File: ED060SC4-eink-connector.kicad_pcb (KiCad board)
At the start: 2 copper layers, 34.9 x 101.6 mm, 2 parts, among them J1 ED060SC4, J2 Conn_01x39_Pin

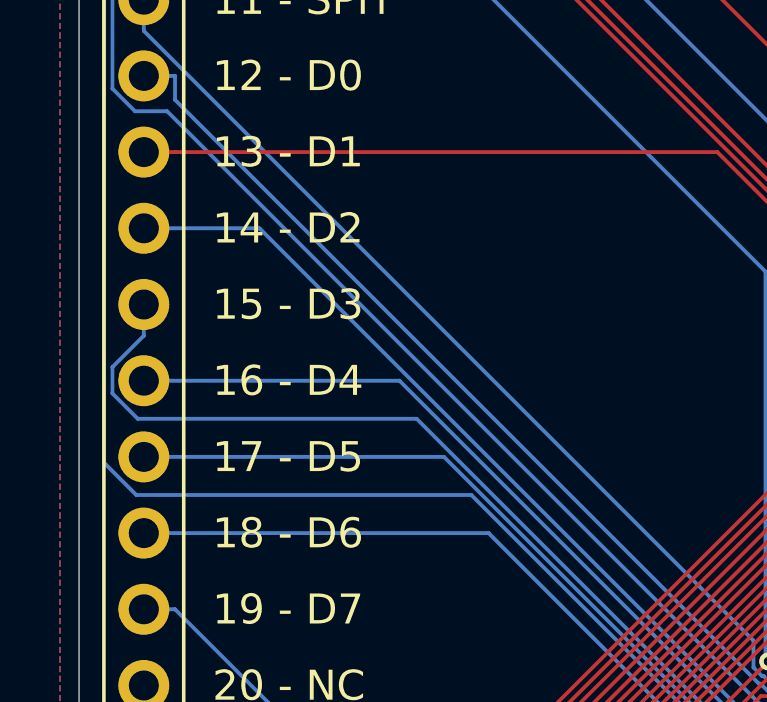
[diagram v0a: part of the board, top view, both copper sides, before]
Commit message: Add a few vias for ground plane
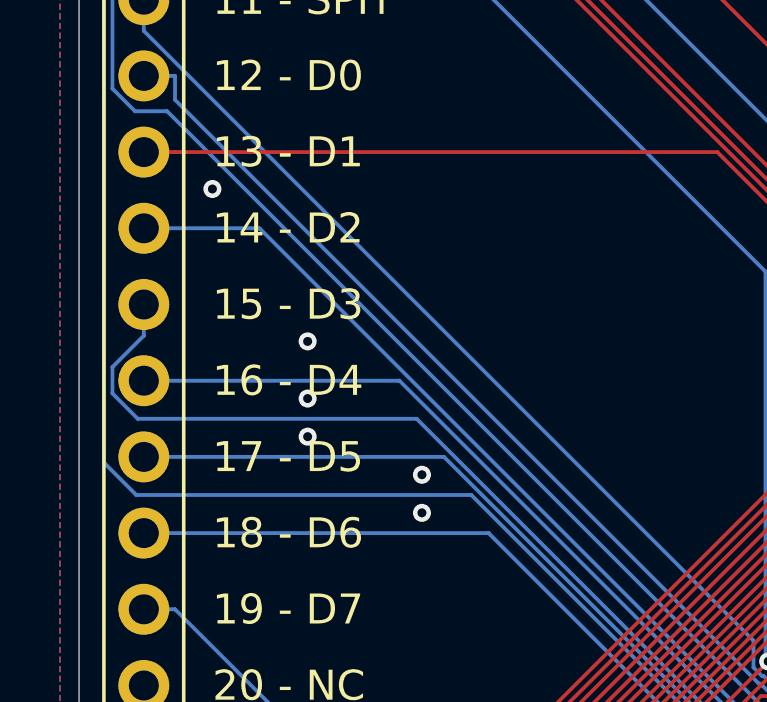
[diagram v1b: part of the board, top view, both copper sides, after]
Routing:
- net /GND: vias 4 -> 10
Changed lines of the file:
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@@
   (segment (start 137.8341 78.9707) (end 137.8341 93.1065) (width 0.127) (layer "F.Cu") (net 6))
   (segment (start 106.934 47.03) (end 106.934 48.0706) (width 0.127) (layer "F.Cu") (net 6))
+  (via (at 116.205 84.455) (size 0.6) (drill 0.3) (layers "F.Cu" "B.Cu") (free) (net 6))
   (via (at 120.65 114.935) (size 0.6) (drill 0.3) (layers "F.Cu" "B.Cu") (free) (net 6))
   (via (at 132.715 67.31) (size 0.6) (drill 0.3) (layers "F.Cu" "B.Cu") (free) (net 6))
+  (via (at 112.395 80.645) (size 0.6) (drill 0.3) (layers "F.Cu" "B.Cu") (free) (net 6))
   (via (at 120.015 113.03) (size 0.6) (drill 0.3) (layers "F.Cu" "B.Cu") (free) (net 6))
+  (via (at 112.395 78.74) (size 0.6) (drill 0.3) (layers "F.Cu" "B.Cu") (free) (net 6))
+  (via (at 116.205 83.185) (size 0.6) (drill 0.3) (layers "F.Cu" "B.Cu") (free) (net 6))
+  (via (at 109.22 73.66) (size 0.6) (drill 0.3) (layers "F.Cu" "B.Cu") (free) (net 6))
+  (via (at 112.395 81.915) (size 0.6) (drill 0.3) (layers "F.Cu" "B.Cu") (free) (net 6))
   (via (at 118.11 112.395) (size 0.6) (drill 0.3) (layers "F.Cu" "B.Cu") (free) (net 6))
   (segment (start 105.8933 42.929) (end 105.8933 40.9464) (width 0.127) (layer "F.Cu") (net 7))

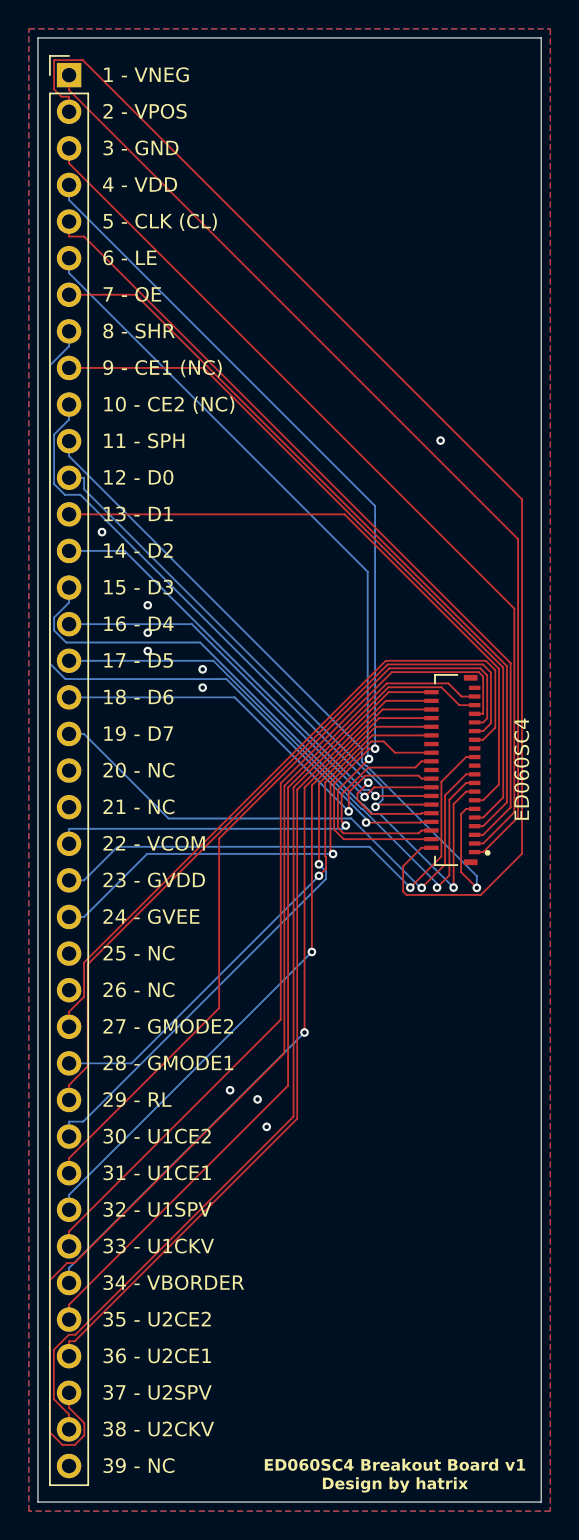
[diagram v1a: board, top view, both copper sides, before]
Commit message: Add mounting holes
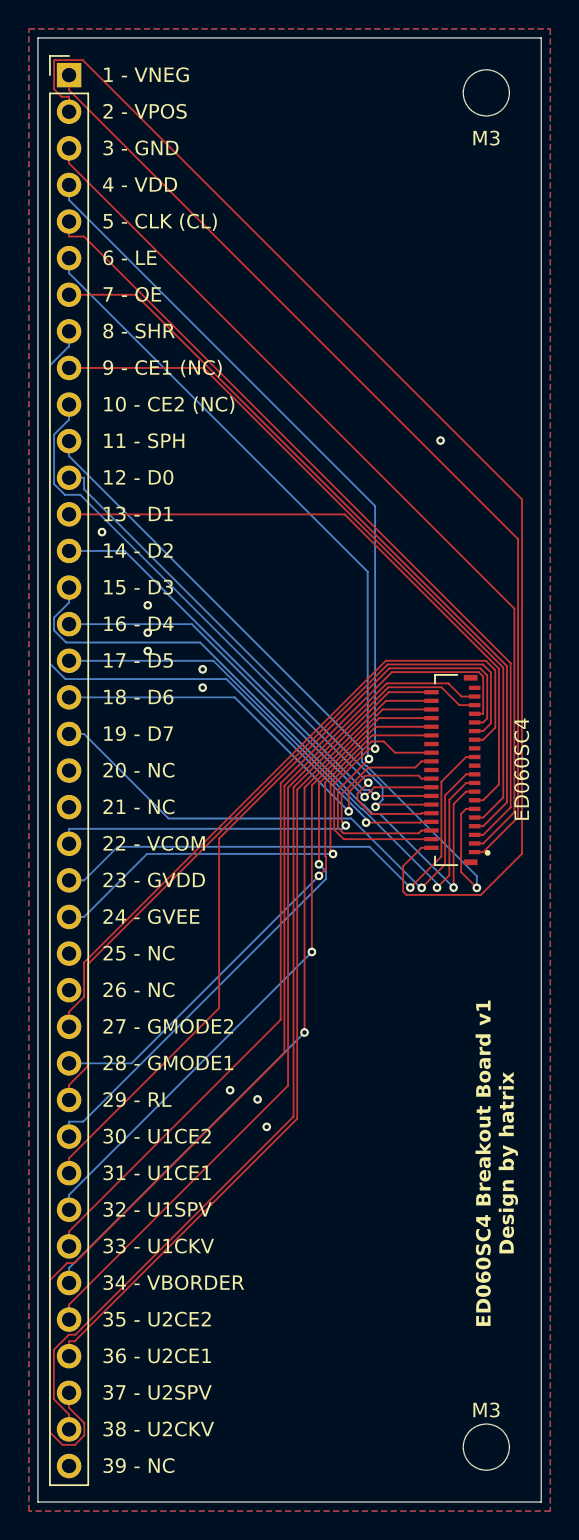
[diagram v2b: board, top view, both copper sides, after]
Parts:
- added M3: MountingHole_3.2mm_M3, MountingHole:MountingHole_3.2mm_M3, F.Cu at (135.9, 137.2)
- added M3: MountingHole_3.2mm_M3, MountingHole:MountingHole_3.2mm_M3, F.Cu at (135.9, 43.2)
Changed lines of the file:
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@@
     )
+  )
+  (footprint "MountingHole:MountingHole_3.2mm_M3" (layer "F.Cu")
+    (at 135.89 137.16)
+    (descr "Mounting Hole 3.2mm, no annular, M3")
+    (tags "mounting hole 3.2mm no annular m3")
+    (attr exclude_from_pos_files exclude_from_bom)
+    (fp_text reference "M3" (at 0 -2.54) (layer "F.SilkS")
+        (effects (font (size 1 1) (thickness 0.15)))
+    )
+    (fp_text value "MountingHole_3.2mm_M3" (at 0 4.2) (layer "F.Fab") hide
+        (effects (font (size 1 1) (thickness 0.15)))
+    )
+    (fp_text user "${REFERENCE}" (at 0 0) (layer "F.Fab")
+        (effects (font (size 1 1) (thickness 0.15)))
+    )
+    (fp_circle (center 0 0) (end 3.2 0)
+      (stroke (width 0.15) (type solid)) (fill none) (layer "Cmts.User"))
+    (fp_circle (center 0 0) (end 3.45 0)
+      (stroke (width 0.05) (type solid)) (fill none) (layer "F.CrtYd"))
+    (pad "" np_thru_hole circle (at 0 0) (size 3.2 3.2) (drill 3.2) (layers "*.Cu" "*.Mask"))
+  )
+  (footprint "MountingHole:MountingHole_3.2mm_M3" (layer "F.Cu")
+    (at 135.89 43.18)
+    (descr "Mounting Hole 3.2mm, no annular, M3")
+    (tags "mounting hole 3.2mm no annular m3")
+    (attr exclude_from_pos_files exclude_from_bom)
+    (fp_text reference "M3" (at 0 3.175) (layer "F.SilkS")
+        (effects (font (size 1 1) (thickness 0.15)))
+    )
+    (fp_text value "MountingHole_3.2mm_M3" (at 0 4.2) (layer "F.Fab") hide
+        (effects (font (size 1 1) (thickness 0.15)))
+    )
+    (fp_text user "${REFERENCE}" (at 0 0) (layer "F.Fab")
+        (effects (font (size 1 1) (thickness 0.15)))
+    )
+    (fp_circle (center 0 0) (end 3.2 0)
+      (stroke (width 0.15) (type solid)) (fill none) (layer "Cmts.User"))
+    (fp_circle (center 0 0) (end 3.45 0)
+      (stroke (width 0.05) (type solid)) (fill none) (layer "F.CrtYd"))
+    (pad "" np_thru_hole circle (at 0 0) (size 3.2 3.2) (drill 3.2) (layers "*.Cu" "*.Mask"))
   )
   (footprint "Connector_PinHeader_2.54mm:PinHeader_1x39_P2.54mm_Vertical" (layer "F.Cu")
@@
     (effects (font (size 1 1) (thickness 0.15)) (justify left bottom))
   )
-  (gr_text "ED060SC4 Breakout Board v1\nDesign by hatrix" (at 129.54 139.065) (layer "F.SilkS")
-    (effects (font (size 0.8 0.8) (thickness 0.2) bold))
+  (gr_text "ED060SC4 Breakout Board v1\nDesign by hatrix" (at 136.525 117.475 90) (layer "F.SilkS")
+    (effects (font (size 1 1) (thickness 0.2) bold))
   )
   (gr_text "13 - D1" (at 109.22 73.025) (layer "F.SilkS")

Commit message: Add original datasheet name for PIN3 (VSS & GND)
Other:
- board text added: "3 - GND (VSS)"
- board text removed: "3 - GND"
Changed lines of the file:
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@@
     (effects (font (size 1 1) (thickness 0.15)) (justify left bottom))
   )
-  (gr_text "3 - GND" (at 109.22 47.625) (layer "F.SilkS")
+  (gr_text "3 - GND (VSS)" (at 109.22 47.625) (layer "F.SilkS")
     (effects (font (size 1 1) (thickness 0.15)) (justify left bottom))
   )

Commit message: Add custom location for JLCPCB's order number
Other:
- board text added: "JLCJLCJLCJLC"
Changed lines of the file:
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@@
       (psa4output false)
       (plotreference true)
-      (plotvalue false)
+      (plotvalue true)
       (plotinvisibletext false)
       (sketchpadsonfab false)
@@
     (effects (font (size 1 1) (thickness 0.15)) (justify left bottom))
   )
+  (gr_text "JLCJLCJLCJLC" (at 134.2 94.8 90) (layer "F.SilkS")
+    (effects (font (size 0.85 0.85) (thickness 0.1)) (justify left bottom))
+  )
   (gr_text "5 - CLK (CL)" (at 109.22 52.705) (layer "F.SilkS")
